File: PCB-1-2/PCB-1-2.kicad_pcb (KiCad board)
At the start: 4 copper layers, 76.4 x 66.5 mm, 129 parts, among them J1 Bus_PCI_Express_x8, J2 ST STDC14 (Debug Connector), J3 USB4105-GF-A, J4 Conn_01x02_Pin, U1 LTC1298IS8_PBF, U10 INA827AIDGKR, U11 LTC1250CS8-PBF, U12 REF3425MDBVTEP, U13 HI-3585APQI, U14 MAX764ESA, U2 LTC1451IS8-PBF, U3 HI-3110PSIF, U4 FT231XS-R, U5 STM32F103RBT6, U6 STWD100YNXWY3F, U7 ADP7104ACPZ-R7 (v3.3), U8 OPA2187IDGKR, U9 ADP7104ACPZ-R7 (5v), Y1 8MHz Crystal, Y2 ABM8-24.000MHz-10-B1U-T

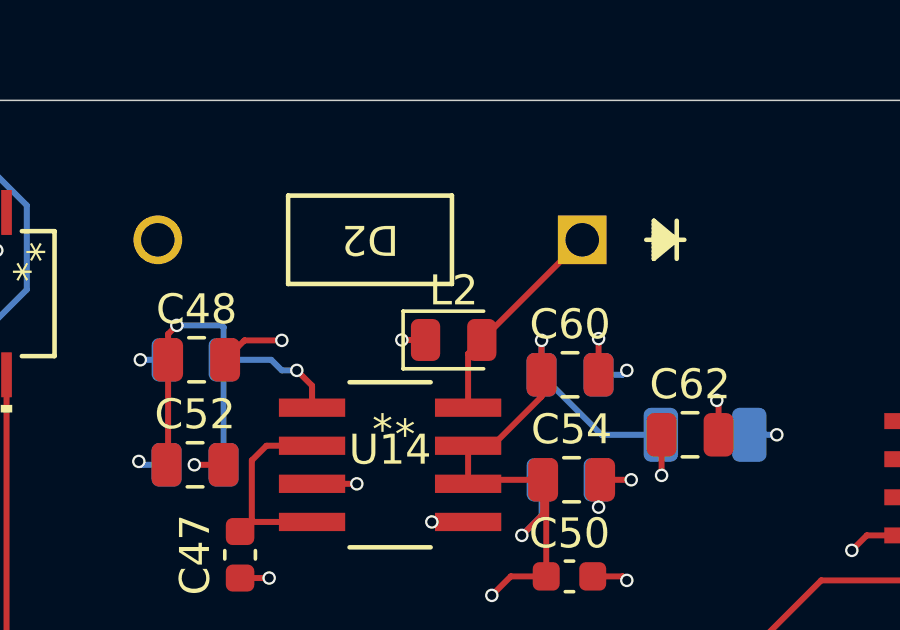
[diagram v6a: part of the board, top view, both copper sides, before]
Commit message: Generated PCB BOM & CSV
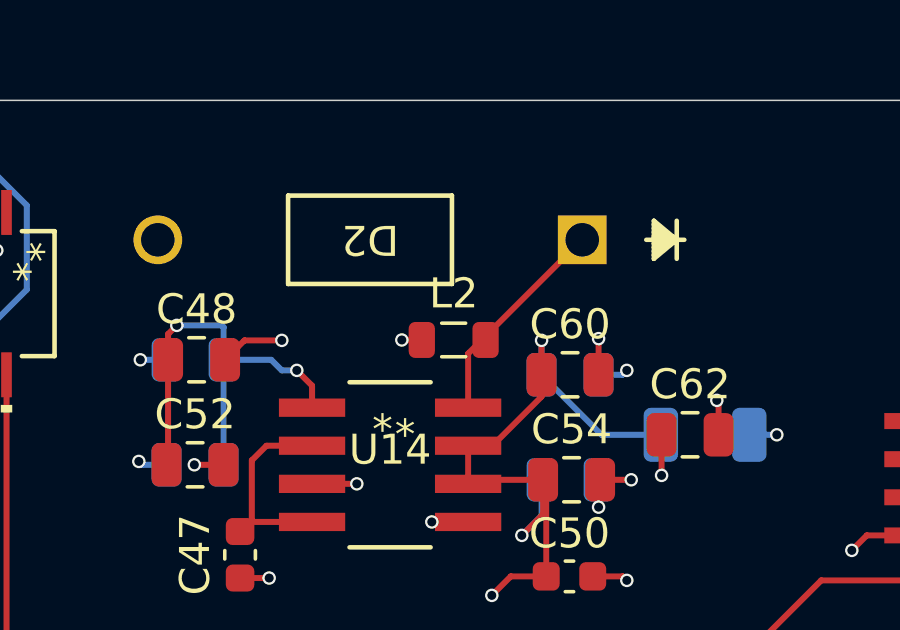
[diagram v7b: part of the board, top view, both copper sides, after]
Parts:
- L2: footprint LED_SMD:LED_0805_2012Metric -> Inductor_SMD:L_0805_2012Metric
- R21: value 5.5k -> 5.6k
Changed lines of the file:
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@@
 			(plot_on_all_layers_selection 0x0000000_00000000)
 			(disableapertmacros no)
-			(usegerberextensions no)
+			(usegerberextensions yes)
 			(usegerberattributes yes)
-			(usegerberadvancedattributes yes)
-			(creategerberjobfile yes)
+			(usegerberadvancedattributes no)
+			(creategerberjobfile no)
 			(dashed_line_dash_ratio 12.000000)
 			(dashed_line_gap_ratio 3.000000)
@@
 			(viasonmask no)
 			(mode 1)
-			(useauxorigin no)
+			(useauxorigin yes)
 			(hpglpennumber 1)
 			(hpglpenspeed 20)
@@
 			(outputformat 1)
 			(mirror no)
-			(drillshape 1)
+			(drillshape 0)
 			(scaleselection 1)
-			(outputdirectory "")
+			(outputdirectory "Files for Production/Gerbers/")
 		)
 	)
@@
 		)
 	)
-	(footprint "LED_SMD:LED_0805_2012Metric"
+	(footprint "Inductor_SMD:L_0805_2012Metric"
 		(layer "F.Cu")
 		(at 102.228496 67.486615)
-		(descr "LED SMD 0805 (2012 Metric), square (rectangular) end terminal, IPC_7351 nominal, (Body size source: https://docs.google.com/spreadsheets/d/1BsfQQcO9C6DZCsRaXUlFlo91Tg2WpOkGARC1WS5S8t0/edit?usp=sharing), generated with kicad-footprint-generator")
-		(tags "LED")
+		(descr "Inductor SMD 0805 (2012 Metric), square (rectangular) end terminal, IPC_7351 nominal, (Body size source: IPC-SM-782 page 80, https://www.pcb-3d.com/wordpress/wp-content/uploads/ipc-sm-782a_amendment_1_and_2.pdf), generated with kicad-footprint-generator")
+		(tags "inductor")
 		(property "Reference" "L2"
-			(at 0 -1.65 0)
+			(at 0 -1.55 0)
 			(layer "F.SilkS")
 			(effects
@@
 		)
 		(property "Value" "47uH"
-			(at 0 1.65 0)
+			(at 0 1.55 0)
 			(layer "F.Fab")
 			(effects
@@
 			)
 		)
-		(property "Footprint" "LED_SMD:LED_0805_2012Metric"
+		(property "Footprint" "Inductor_SMD:L_0805_2012Metric"
 			(at 0 0 0)
 			(unlocked yes)
@@
 		(attr smd)
 		(fp_line
-			(start -1.685 -0.96)
-			(end -1.685 0.96)
+			(start -0.399622 -0.56)
+			(end 0.399622 -0.56)
 			(stroke
 				(width 0.12)
@@
 		)
 		(fp_line
-			(start -1.685 0.96)
-			(end 1 0.96)
+			(start -0.399622 0.56)
+			(end 0.399622 0.56)
 			(stroke
 				(width 0.12)
@@
 		)
 		(fp_line
-			(start 1 -0.96)
-			(end -1.685 -0.96)
-			(stroke
-				(width 0.12)
-				(type solid)
-			)
-			(layer "F.SilkS")
-		)
-		(fp_line
-			(start -1.68 -0.95)
-			(end 1.68 -0.95)
+			(start -1.75 -0.85)
+			(end 1.75 -0.85)
 			(stroke
 				(width 0.05)
@@
 		)
 		(fp_line
-			(start -1.68 0.95)
-			(end -1.68 -0.95)
+			(start -1.75 0.85)
+			(end -1.75 -0.85)
 			(stroke
 				(width 0.05)
@@
 		)
 		(fp_line
-			(start 1.68 -0.95)
-			(end 1.68 0.95)
+			(start 1.75 -0.85)
+			(end 1.75 0.85)
 			(stroke
 				(width 0.05)
@@
 		)
 		(fp_line
-			(start 1.68 0.95)
-			(end -1.68 0.95)
+			(start 1.75 0.85)
+			(end -1.75 0.85)
 			(stroke
 				(width 0.05)
@@
 		)
 		(fp_line
-			(start -1 -0.3)
-			(end -1 0.6)
-			(stroke
-				(width 0.1)
-				(type solid)
-			)
-			(layer "F.Fab")
-		)
-		(fp_line
-			(start -1 0.6)
-			(end 1 0.6)
+			(start -1 -0.45)
+			(end 1 -0.45)
 			(stroke
 				(width 0.1)
@@
 		)
 		(fp_line
-			(start -0.7 -0.6)
-			(end -1 -0.3)
+			(start -1 0.45)
+			(end -1 -0.45)
 			(stroke
 				(width 0.1)
@@
 		)
 		(fp_line
-			(start 1 -0.6)
-			(end -0.7 -0.6)
+			(start 1 -0.45)
+			(end 1 0.45)
 			(stroke
 				(width 0.1)
@@
 		)
 		(fp_line
-			(start 1 0.6)
-			(end 1 -0.6)
+			(start 1 0.45)
+			(end -1 0.45)
 			(stroke
 				(width 0.1)
@@
 		)
 		(pad "1" smd roundrect
-			(at -0.9375 0)
-			(size 0.975 1.4)
+			(at -1.0625 0)
+			(size 0.875 1.2)
 			(layers "F.Cu" "F.Paste" "F.Mask")
 			(roundrect_rratio 0.25)
@@
 		)
 		(pad "2" smd roundrect
-			(at 0.9375 0)
-			(size 0.975 1.4)
+			(at 1.0625 0)
+			(size 0.875 1.2)
 			(layers "F.Cu" "F.Paste" "F.Mask")
 			(roundrect_rratio 0.25)
@@
 			(pintype "passive")
 		)
-		(model "${KICAD8_3DMODEL_DIR}/LED_SMD.3dshapes/LED_0805_2012Metric.wrl"
+		(model "${KICAD8_3DMODEL_DIR}/Inductor_SMD.3dshapes/L_0805_2012Metric.wrl"
 			(offset
 				(xyz 0 0 0)
@@
 			)
 		)
-		(property "Value" "5.5k"
+		(property "Value" "5.6k"
 			(at 0 -1.65 0)
 			(layer "B.Fab")
